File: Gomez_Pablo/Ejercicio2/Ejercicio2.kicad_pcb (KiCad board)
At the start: 2 copper layers, 40.6 x 61 mm, 13 parts, among them J1 DB9, U1 SP3232ECN, U2 AMIS42665TJAA1RG

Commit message: Se sube la versión actualizada del pcb
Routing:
- net GND: track 9.25 -> 56.6 mm, vias 0 -> 13
- added copper zone on B.Cu, net GND
- added copper zone on F.Cu, net GND
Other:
- board text added: "INDUSTRIA ARGENTINA"
- board text added: "INTI - CMNB"
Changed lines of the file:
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@@
   (general
     (links 43)
-    (no_connects 15)
+    (no_connects 0)
     (area 178.359999 78.664999 219.150001 139.775001)
     (thickness 1.6)
-    (drawings 4)
-    (tracks 137)
+    (drawings 6)
+    (tracks 169)
     (zones 0)
     (modules 13)
@@
   (layers
     (0 F.Cu signal)
-    (31 B.Cu signal)
+    (31 B.Cu signal hide)
     (32 B.Adhes user)
     (33 F.Adhes user)
@@
     (user_trace_width 0.3048)
     (trace_clearance 0.2)
-    (zone_clearance 0.508)
-    (zone_45_only no)
+    (zone_clearance 0.2032)
+    (zone_45_only yes)
     (trace_min 0.2)
     (segment_width 0.2)
@@
     (pad 2 smd rect (at 2 0) (size 2 1.7) (layers B.Cu B.Paste B.Mask)
       (net 20 "Net-(R1-Pad2)"))
-    (model Resistors_SMD.3dshapes/R_1206_HandSoldering.wrl
+    (model ${KIPRJMOD}/ej2.3dshapes/R_1206_HandSoldering.wrl
       (at (xyz 0 0 0))
       (scale (xyz 1 1 1))
@@
     (pad 2 smd rect (at 2 0 180) (size 2 1.7) (layers B.Cu B.Paste B.Mask)
       (net 19 "Net-(JP1-Pad2)"))
-    (model Resistors_SMD.3dshapes/R_1206_HandSoldering.wrl
+    (model ${KIPRJMOD}/ej2.3dshapes/R_1206_HandSoldering.wrl
       (at (xyz 0 0 0))
       (scale (xyz 1 1 1))
@@
     (pad 2 smd rect (at 2 0 270) (size 2 1.6) (layers F.Cu F.Paste F.Mask)
       (net 2 "Net-(C1-Pad2)"))
+    (model ${KIPRJMOD}/ej2.3dshapes/C_1206_HandSoldering.wrl
+      (at (xyz 0 0 0))
+      (scale (xyz 1 1 1))
+      (rotate (xyz 0 0 0))
+    )
   )
   (module ej2:C_1206_Handsoldering (layer F.Cu)
@@
     (pad 2 smd rect (at 2 0 270) (size 2 1.6) (layers F.Cu F.Paste F.Mask)
       (net 4 "Net-(C2-Pad2)"))
+    (model ${KIPRJMOD}/ej2.3dshapes/C_1206_HandSoldering.wrl
+      (at (xyz 0 0 0))
+      (scale (xyz 1 1 1))
+      (rotate (xyz 0 0 0))
+    )
   )
   (module ej2:C_1206_Handsoldering (layer F.Cu)
@@
     (pad 2 smd rect (at 2 0) (size 2 1.6) (layers F.Cu F.Paste F.Mask)
       (net 6 "Net-(C3-Pad2)"))
+    (model ${KIPRJMOD}/ej2.3dshapes/C_1206_HandSoldering.wrl
+      (at (xyz 0 0 0))
+      (scale (xyz 1 1 1))
+      (rotate (xyz 0 0 0))
+    )
   )
   (module ej2:C_1206_Handsoldering (layer F.Cu)
@@
     (pad 2 smd rect (at 2 0 180) (size 2 1.6) (layers F.Cu F.Paste F.Mask)
       (net 7 "Net-(C4-Pad2)"))
+    (model ${KIPRJMOD}/ej2.3dshapes/C_1206_HandSoldering.wrl
+      (at (xyz 0 0 0))
+      (scale (xyz 1 1 1))
+      (rotate (xyz 0 0 0))
+    )
   )
   (module ej2:C_1206_Handsoldering (layer F.Cu)
@@
     (pad 2 smd rect (at 2 0) (size 2 1.6) (layers F.Cu F.Paste F.Mask)
       (net 8 +3.3V))
+    (model ${KIPRJMOD}/ej2.3dshapes/C_1206_HandSoldering.wrl
+      (at (xyz 0 0 0))
+      (scale (xyz 1 1 1))
+      (rotate (xyz 0 0 0))
+    )
   )
   (module ej2:C_1206_Handsoldering (layer F.Cu)
@@
     (pad 2 smd rect (at 2 0) (size 2 1.6) (layers F.Cu F.Paste F.Mask)
       (net 27 +5V))
+    (model ${KIPRJMOD}/ej2.3dshapes/C_1206_HandSoldering.wrl
+      (at (xyz 0 0 0))
+      (scale (xyz 1 1 1))
+      (rotate (xyz 0 0 0))
+    )
+  )
+  (gr_text "INDUSTRIA ARGENTINA" (at 192.405 137.16) (layer B.Mask)
+    (effects (font (size 1.5 1.5) (thickness 0.3)) (justify mirror))
+  )
+  (gr_text "INTI - CMNB" (at 187.325 133.35) (layer F.SilkS)
+    (effects (font (size 1.5 1.5) (thickness 0.3)))
   )
   (gr_line (start 219.075 139.7) (end 219.075 78.74) (angle 90) (layer Edge.Cuts) (width 0.15))
@@
   (segment (start 194.945 106.045) (end 192.405 108.585) (width 0.3048) (layer F.Cu) (net 4))
   (segment (start 192.405 108.585) (end 192.405 109.315) (width 0.3048) (layer F.Cu) (net 4))
+  (segment (start 199.39 112.395) (end 196.215 112.395) (width 0.3048) (layer B.Cu) (net 5))
+  (via (at 199.39 112.395) (size 0.6) (drill 0.4) (layers F.Cu B.Cu) (net 5))
+  (segment (start 201.39 112.395) (end 199.39 112.395) (width 0.3048) (layer F.Cu) (net 5))
+  (via (at 182.245 114.935) (size 0.6) (drill 0.4) (layers F.Cu B.Cu) (net 5))
+  (segment (start 183.515 114.935) (end 182.245 114.935) (width 0.3048) (layer F.Cu) (net 5))
+  (via (at 183.515 114.935) (size 0.6) (drill 0.4) (layers F.Cu B.Cu) (net 5))
+  (segment (start 184.785 114.935) (end 183.515 114.935) (width 0.3048) (layer B.Cu) (net 5))
+  (via (at 184.785 114.935) (size 0.6) (drill 0.4) (layers F.Cu B.Cu) (net 5))
+  (segment (start 186.055 114.935) (end 184.785 114.935) (width 0.3048) (layer F.Cu) (net 5))
+  (via (at 186.055 114.935) (size 0.6) (drill 0.4) (layers F.Cu B.Cu) (net 5))
+  (segment (start 193.675 114.935) (end 186.055 114.935) (width 0.3048) (layer B.Cu) (net 5))
+  (segment (start 196.215 112.395) (end 193.675 114.935) (width 0.3048) (layer B.Cu) (net 5))
+  (segment (start 196.755 121.285) (end 196.755 121.38) (width 0.3048) (layer F.Cu) (net 5))
+  (segment (start 196.755 121.38) (end 191.135 127) (width 0.3048) (layer F.Cu) (net 5))
+  (via (at 191.135 127) (size 0.6) (drill 0.4) (layers F.Cu B.Cu) (net 5))
+  (segment (start 191.135 127) (end 189.865 127) (width 0.3048) (layer B.Cu) (net 5))
+  (segment (start 189.865 127) (end 191.135 127) (width 0.3048) (layer B.Cu) (net 5))
+  (segment (start 191.135 127) (end 189.865 127) (width 0.3048) (layer B.Cu) (net 5))
+  (via (at 189.865 127) (size 0.6) (drill 0.4) (layers F.Cu B.Cu) (net 5))
+  (segment (start 189.865 127) (end 189.865 128.27) (width 0.3048) (layer F.Cu) (net 5))
+  (via (at 189.865 128.27) (size 0.6) (drill 0.4) (layers F.Cu B.Cu) (net 5))
+  (segment (start 189.865 128.27) (end 191.135 128.27) (width 0.3048) (layer B.Cu) (net 5))
+  (via (at 191.135 128.27) (size 0.6) (drill 0.4) (layers F.Cu B.Cu) (net 5))
+  (segment (start 197.485 85.09) (end 198.755 85.09) (width 0.3048) (layer F.Cu) (net 5))
+  (segment (start 198.755 86.36) (end 198.755 85.09) (width 0.3048) (layer F.Cu) (net 5))
+  (via (at 198.755 85.09) (size 0.6) (drill 0.4) (layers F.Cu B.Cu) (net 5))
+  (segment (start 197.39 86.455) (end 197.39 95.25) (width 0.3048) (layer F.Cu) (net 5))
+  (segment (start 197.485 86.36) (end 198.755 86.36) (width 0.3048) (layer B.Cu) (net 5))
+  (via (at 197.485 86.36) (size 0.6) (drill 0.4) (layers F.Cu B.Cu) (net 5))
+  (segment (start 197.39 86.455) (end 197.485 86.36) (width 0.3048) (layer F.Cu) (net 5))
+  (via (at 198.755 86.36) (size 0.6) (drill 0.4) (layers F.Cu B.Cu) (net 5))
+  (via (at 197.485 85.09) (size 0.6) (drill 0.4) (layers F.Cu B.Cu) (net 5))
   (segment (start 195.58 96.52) (end 195.58 95.25) (width 0.3048) (layer F.Cu) (net 5))
   (segment (start 195.58 95.25) (end 197.39 95.25) (width 0.3048) (layer F.Cu) (net 5))
@@
   (segment (start 191.77 117.475) (end 196.055 117.475) (width 0.3048) (layer F.Cu) (net 18))
   (segment (start 187.325 121.92) (end 191.77 117.475) (width 0.3048) (layer F.Cu) (net 18))
-  (segment (start 196.055 116.205) (end 196.85 116.205) (width 0.3048) (layer F.Cu) (net 19) (status 400000))
-  (segment (start 197.485 115.57) (end 195.485 115.57) (width 0.3048) (layer B.Cu) (net 19) (status 800000))
+  (segment (start 196.055 116.205) (end 196.85 116.205) (width 0.3048) (layer F.Cu) (net 19))
+  (segment (start 197.485 115.57) (end 195.485 115.57) (width 0.3048) (layer B.Cu) (net 19))
   (via (at 197.485 115.57) (size 0.6) (drill 0.4) (layers F.Cu B.Cu) (net 19))
   (segment (start 196.85 116.205) (end 197.485 115.57) (width 0.3048) (layer F.Cu) (net 19))
@@
   (segment (start 189.23 116.205) (end 196.055 116.205) (width 0.3048) (layer F.Cu) (net 19))
   (segment (start 186.055 119.38) (end 189.23 116.205) (width 0.3048) (layer F.Cu) (net 19))
-  (segment (start 199.485 115.57) (end 199.485 118.11) (width 0.3048) (layer B.Cu) (net 20) (status C00000))
+  (segment (start 199.485 115.57) (end 199.485 118.11) (width 0.3048) (layer B.Cu) (net 20))
   (segment (start 199.485 118.11) (end 198.755 118.11) (width 0.3048) (layer B.Cu) (net 20))
   (segment (start 198.755 118.11) (end 197.485 116.84) (width 0.3048) (layer B.Cu) (net 20))
@@
   (segment (start 199.39 116.84) (end 200.025 116.205) (width 0.3048) (layer F.Cu) (net 27))
   (segment (start 200.025 116.205) (end 201.455 116.205) (width 0.3048) (layer F.Cu) (net 27))
+  (zone (net 5) (net_name GND) (layer B.Cu) (hatch edge 0.508)
+    (connect_pads (clearance 0.2032))
+    (min_thickness 0.2032)
+    (fill yes (arc_segments 32) (thermal_gap 0.2032) (thermal_bridge_width 0.508))
+    (polygon
+      (pts
+        (xy 178.435 139.7) (xy 178.435 78.74) (xy 219.075 78.74) (xy 219.075 139.7)
+      )
+    )
+    (polygon
+      (pts        (xy 179.705 135.255) (xy 179.705 139.065) (xy 205.105 139.065) (xy 205.105 135.255)
+      )
+    )
+  )
+  (zone (net 5) (net_name GND) (layer F.Cu) (hatch edge 0.508)
+    (connect_pads (clearance 0.2032))
+    (min_thickness 0.2032)
+    (fill yes (arc_segments 32) (thermal_gap 0.2032) (thermal_bridge_width 0.508))
+    (polygon
+      (pts
+        (xy 178.435 139.7) (xy 178.435 78.74) (xy 219.075 78.74) (xy 219.075 139.7)
+      )
+    )
+  )
+  (zone (net 0) (net_name "") (layer F.Cu) (hatch edge 0.508)
+    (connect_pads (clearance 0.2032))
+    (min_thickness 0.2032)
+    (keepout (tracks allowed) (vias not_allowed) (copperpour not_allowed))
+    (fill yes (arc_segments 32) (thermal_gap 0.2032) (thermal_bridge_width 0.508))
+    (polygon
+      (pts
+        (xy 194.945 114.3) (xy 193.675 115.57) (xy 187.325 115.57) (xy 184.785 118.11) (xy 179.705 118.11)
+        (xy 179.705 124.46) (xy 187.325 124.46) (xy 189.865 124.46) (xy 194.945 119.38)
+      )
+    )
+  )
 )

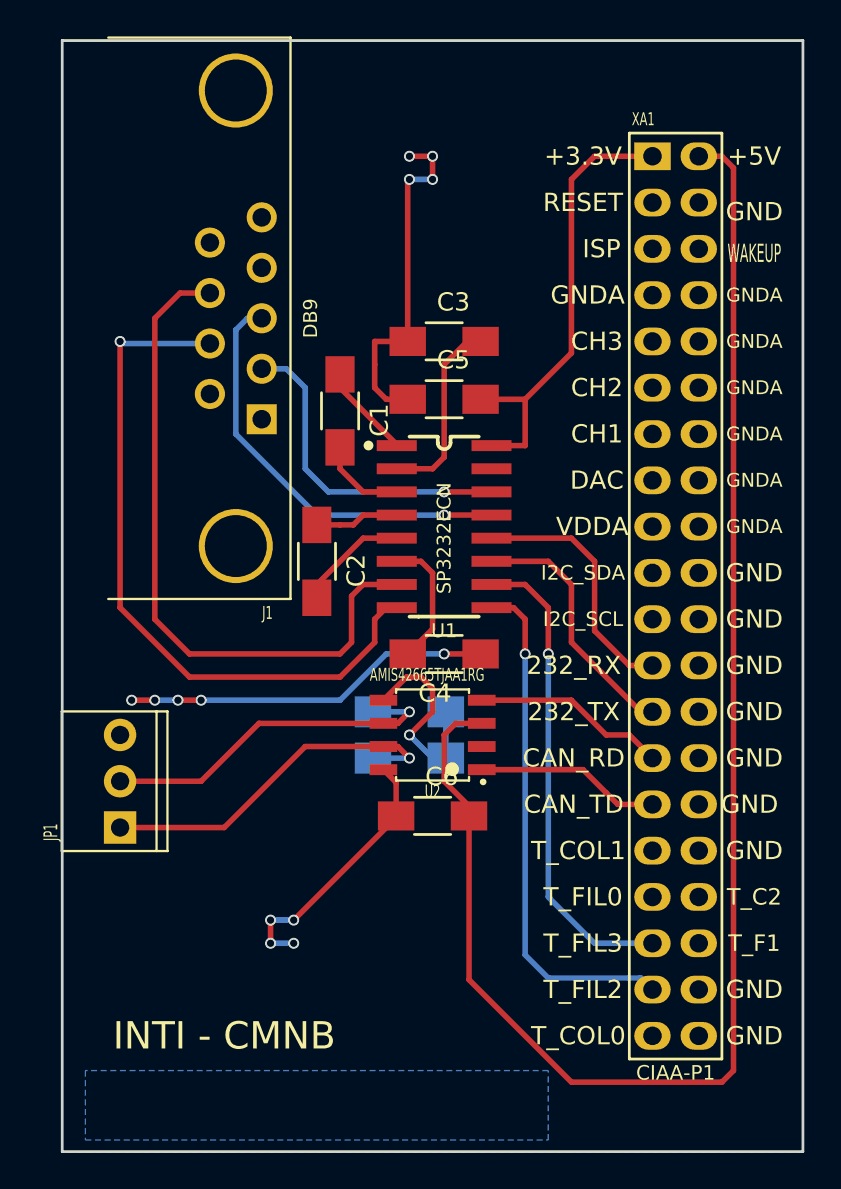
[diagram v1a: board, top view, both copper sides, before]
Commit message: se ecualizan pares diferenciales
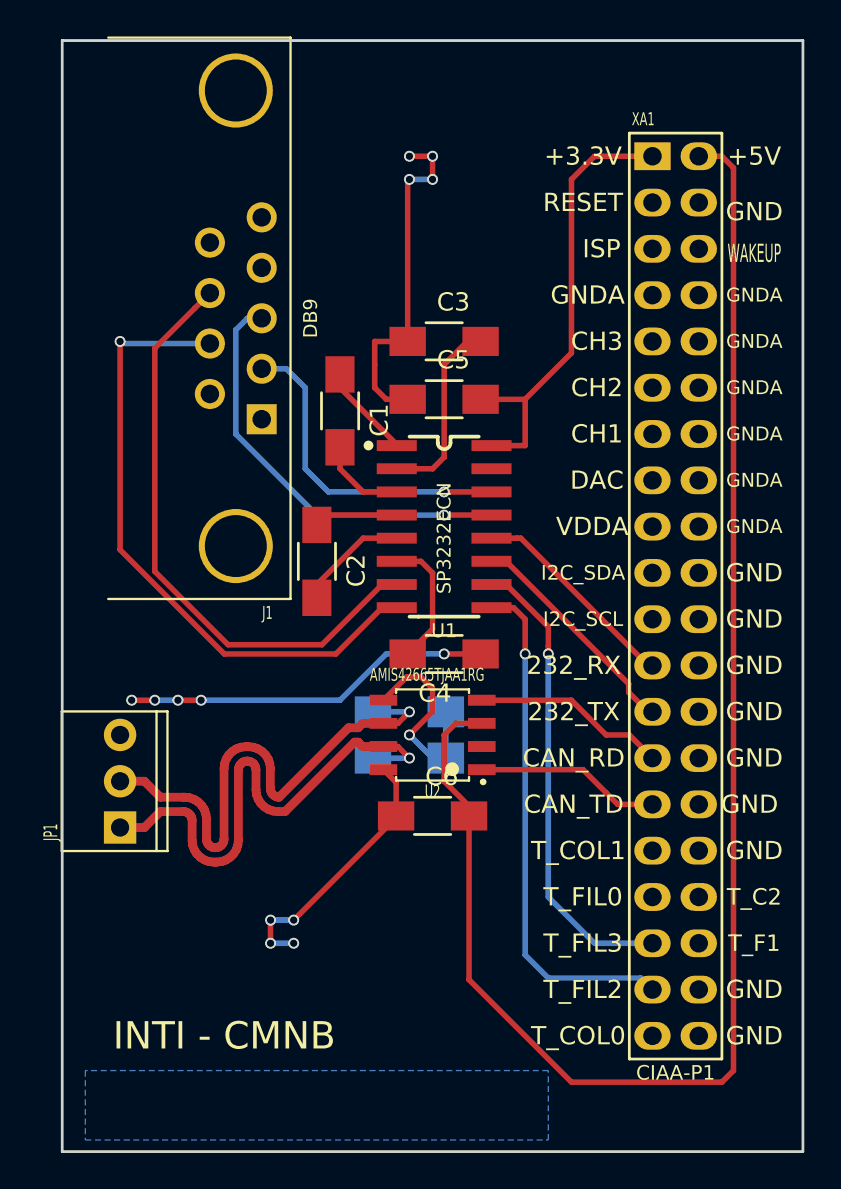
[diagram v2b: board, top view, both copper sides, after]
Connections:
- net Net-(JP1-Pad1) renamed /Conector/CAN_P
- net Net-(JP1-Pad2) renamed /Conector/CAN_N
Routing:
- net /Conector/CAN_N: track 19.5 -> 29.1 mm
- net /Conector/CAN_P: track 20.0 -> 29.1 mm
- net Net-(J1-Pad8): track 37.2 -> 32.8 mm
- net Net-(J1-Pad7): track 38.7 -> 35.6 mm
- net /Conector/TXD: track 14.0 -> 11.7 mm
- net /Conector/RXD: track 14.1 -> 13.2 mm
- net /Conector/CTS: track 26.3 -> 25.7 mm
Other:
- board text added: "1 Oz"
- board text added: "1,6 mm"
- board text added: "Dieléctrico"
- board text added: "Espesor final: 1,6 mm"
- board text added: "L1 TOP (mixed)"
- board text added: "L2 TOP (mixed)"
- board text added: "Terminación: HASL"
